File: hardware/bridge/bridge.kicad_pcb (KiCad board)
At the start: 2 copper layers, 45 x 80 mm, 58 parts, among them J1 XT30U-M, J2 Seg A, J3 Seg B, J4 Seg C, J5 Seg D, J6 Head, J7 OLED, J8 Shutdown button, J9 Ext 5V, Q1 NCE40P70K, U1 LMR51606XDBVR, U2 WeAct STM32G474 QFN48, U3 LSM6DSV16X breakout

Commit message: Bridge PCB: soft power switch, PA5 breakout, time-lag fuses
- Soft power switch: Q2 grounds the soft start's R1, so the button (J8,
  now BTN_A and BTN_B) or the bridge's PC4 hold turns the robot on. A
  stretch RC lets a tap last until the bridge has booted; Q3 gives PB5 an
  active-low button sense with no battery voltage on the pin; Q5 and Q4
  snap Q1 off in about 20 ms. Off leaves about 20 uA. JP2, open, bridges
  back to the old always-on behaviour.
- PA5 breakout pads (G 5V 3V3 A5) in the bottom-left corner, name block
  moved below them.
- Data-line zener footprints D4 to D7 dropped to make room; never fitted.
- Segment B and D feeds get a second via at their layer change; SEG C's
  feed runs round the board edge so it no longer walls off the bottom
  layer.
- Fuses changed to BHFUSE BSMD1206C time-lag parts: the Littelfuse 0458s
  were very fast-acting.
- JLC package, PDFs and 3D render regenerated; design note updated
  (docs/bridge-pcb.md section 6.5 has the firmware rules).
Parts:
- removed D4, D5, D6, D7: BZT52C5V6S, Diode_SMD:D_SOD-323
- added C14: 1u 50V, Capacitor_SMD:C_0603_1608Metric, F.Cu at (105.6, 78.9)
- added D11: BAT54WS, Diode_SMD:D_SOD-323, F.Cu at (119.8, 83.9)
- added D12: 1N4148WS, Diode_SMD:D_SOD-323, F.Cu at (102.2, 76.5)
- added D13: BZT52C12S, Diode_SMD:D_SOD-323, F.Cu at (116.1, 83.9)
- added D9: BZT52C12S, Diode_SMD:D_SOD-323, F.Cu at (106.1, 72.0)
- added J10: PA5 breakout, Connector_PinHeader_2.54mm:PinHeader_1x04_P2.54mm_Vertical, F.Cu at (102.0, 115.8)
- added JP2: bridge = always on, Jumper:SolderJumper-2_P1.3mm_Open_RoundedPad1.0x1.5mm, F.Cu at (124.0, 68.6)
- added Q2: 2N7002, Package_TO_SOT_SMD:SOT-23, F.Cu at (120.5, 73.4)
- added Q3: 2N7002, Package_TO_SOT_SMD:SOT-23, F.Cu at (102.3, 73.0)
- added Q4: MMBT3906, Package_TO_SOT_SMD:SOT-23, F.Cu at (112.7, 73.4)
- added Q5: 2N7002, Package_TO_SOT_SMD:SOT-23, F.Cu at (116.6, 73.4)
- added R13: 1M, Resistor_SMD:R_0603_1608Metric, F.Cu at (112.5, 83.7)
- added R14: 470k, Resistor_SMD:R_0603_1608Metric, F.Cu at (105.8, 76.3)
- added R15: 1M, Resistor_SMD:R_0603_1608Metric, F.Cu at (102.1, 78.9)
- added R20: 1M, Resistor_SMD:R_0603_1608Metric, F.Cu at (119.4, 81.6)
- added R21: 2.2M, Resistor_SMD:R_0603_1608Metric, F.Cu at (116.0, 81.6)
- added R22: 1M, Resistor_SMD:R_0603_1608Metric, F.Cu at (112.5, 81.6)
- J8: value Shutdown button -> Power button
- moved R12 7.31 mm to (102.1, 81.1)
- moved D1 7.29 mm to (113.4, 77.1)
- moved C13 7.28 mm to (105.6, 81.1)
- moved R3 7.03 mm to (119.4, 79.6)
- moved R7 6.35 mm to (105.6, 83.2)
- moved R5 5.88 mm to (109.0, 81.1)
- moved R11 5.81 mm to (109.0, 78.9)
- moved D3 5.26 mm to (103.3, 70.1)
- moved R4 5.25 mm to (103.3, 68.2)
- moved C2 3.22 mm to (116.0, 79.6)
- moved R1 2.98 mm to (112.5, 79.6)
- moved R2 2.72 mm to (121.6, 76.7)
- moved R8 2.60 mm to (109.0, 83.2)
- moved R6 2.50 mm to (102.1, 83.2)
- moved C1 2.03 mm to (117.9, 76.9)
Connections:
- J8 pad 1: /BTN -> /BTN_A
- J8 pad 2: GND -> /BTN_B
- R1 pad 2: GND -> /PWR_LO
- U2 pad 36: unconnected-(U2-PC4-Pad36) -> /PWR_HOLD
- U2 pad 37: unconnected-(U2-PA5-Pad37) -> /PA5_IO
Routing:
- net /VHEAD: track 117.2 -> 45.0 mm, vias 4 -> 3
- net /PWR_ON: track 0.00 -> 47.6 mm, vias 0 -> 2
- net /VBAT_F: track 31.5 -> 72.7 mm, vias 4 -> 9
- net /PA5_IO: track 0.00 -> 32.4 mm
- net /BTN_B: track 0.00 -> 29.9 mm, vias 0 -> 1
- net GND: track 284.4 -> 310.4 mm, vias 225 -> 210
- net /LINK_RX: track 99.7 -> 76.5 mm, vias 2 -> 3
- net /PWR_LO: track 0.00 -> 22.3 mm, vias 0 -> 2
- net /Q4_B: track 0.00 -> 16.5 mm, vias 0 -> 2
- net /LINK_TX: track 72.9 -> 89.1 mm
- net +5V: track 44.5 -> 60.4 mm
- net /Q5_G: track 0.00 -> 15.4 mm
- net /OLED_SDA: track 77.9 -> 92.4 mm, vias 4 -> 5
- net /SEG_A: track 46.1 -> 59.8 mm
- net /VBAT_SENSE: track 59.8 -> 47.3 mm, vias 4 -> 1
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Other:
- board text added: "3V3"
- board text added: "A5"
- board text added: "ALWAYS ON"
- board text added: "BRIDGE FOR"

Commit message: Bridge PCB: head feed fuse F6 raised to 2 A
The head carrier's 5 V, 3 A buck draws about 0.85 A from a nearly flat
pack before amplifier peaks, too close to a 1 A rating. F6 is now the
BSMD1206C-1200T (C41367223), same 1206 footprint; fab outputs and the
schematic PDF regenerated, ERC clean.
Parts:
- F6: value 1A -> 2A
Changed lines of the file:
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@@
 			)
 		)
-		(property "Value" "1A"
+		(property "Value" "2A"
 			(at 0 1.83 0)
 			(layer "F.Fab")
@@
 			)
 		)
-		(property "LCSC" "C41367221"
+		(property "LCSC" "C41367223"
 			(at 0 0 0)
 			(layer "F.SilkS")
@@
 			)
 		)
-		(property "MPN" "BHFUSE BSMD1206C-1100T, 1 A time lag, 72 V DC"
+		(property "MPN" "BHFUSE BSMD1206C-1200T, 2 A time lag, 72 V DC"
 			(at 0 0 0)
 			(layer "F.SilkS")

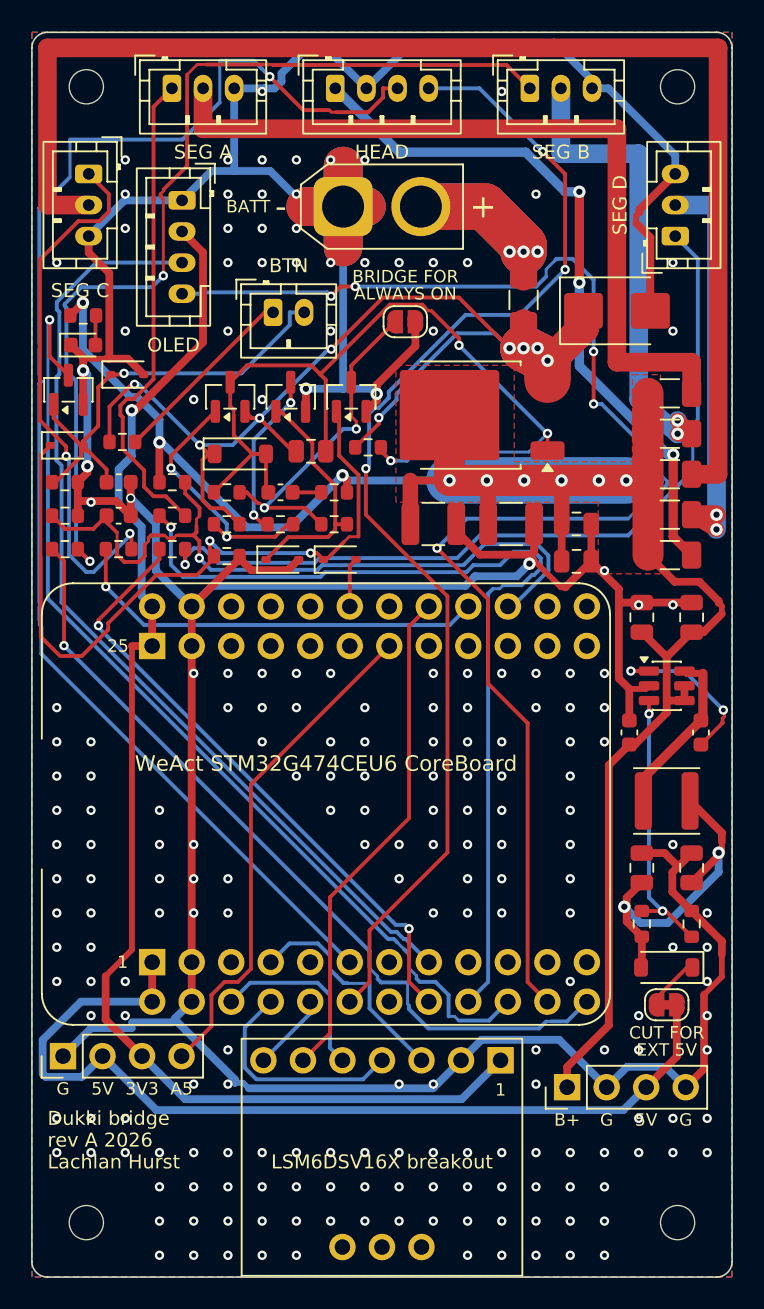
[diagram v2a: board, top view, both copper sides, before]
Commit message: Bridge PCB rev B: WeAct header fix and pre-order review changes
- WeAct footprint: the VCC-side header (P1) had its rows swapped. The
  generator put odd pins on the inner row of both headers, but the two
  headers are the same part placed the same way round, so P1's odd pins
  are on its outer row (confirmed on the board: PB13 is on P1's inner
  row). Every P1 signal would have met its column neighbour.
- J7 (display) is now a 5-pin PH so the 4-pin head cable cannot go in it.
- C15, 1 uF X7R on PWR_ON: holds the power switch through a bridge reset
  and stretches a tap; C14 now X7R 0805, R14 220k.
- L1 SWPA6045S330MT (1.65 A saturation), D2 SMBJ26A (C19077580,
  Preferred).
- Buck column re-laid in current order; bulk capacitors stood on end
  under Q1; power capacitor ground pads solid; head feed VHEAD in a
  1.0 mm class.
- JP1 turned 180 degrees with hand-drawn links, and a top-layer keep-out
  across its cut line (no tracks, vias or pour).
- NYLON marked at H1 and H2 (segment C's feed runs under their heads).
- Routing tidied with tidy_head_pcb.py; DRC clean with schematic parity.
  JLC package, PDFs and render regenerated; design note section 6.6.
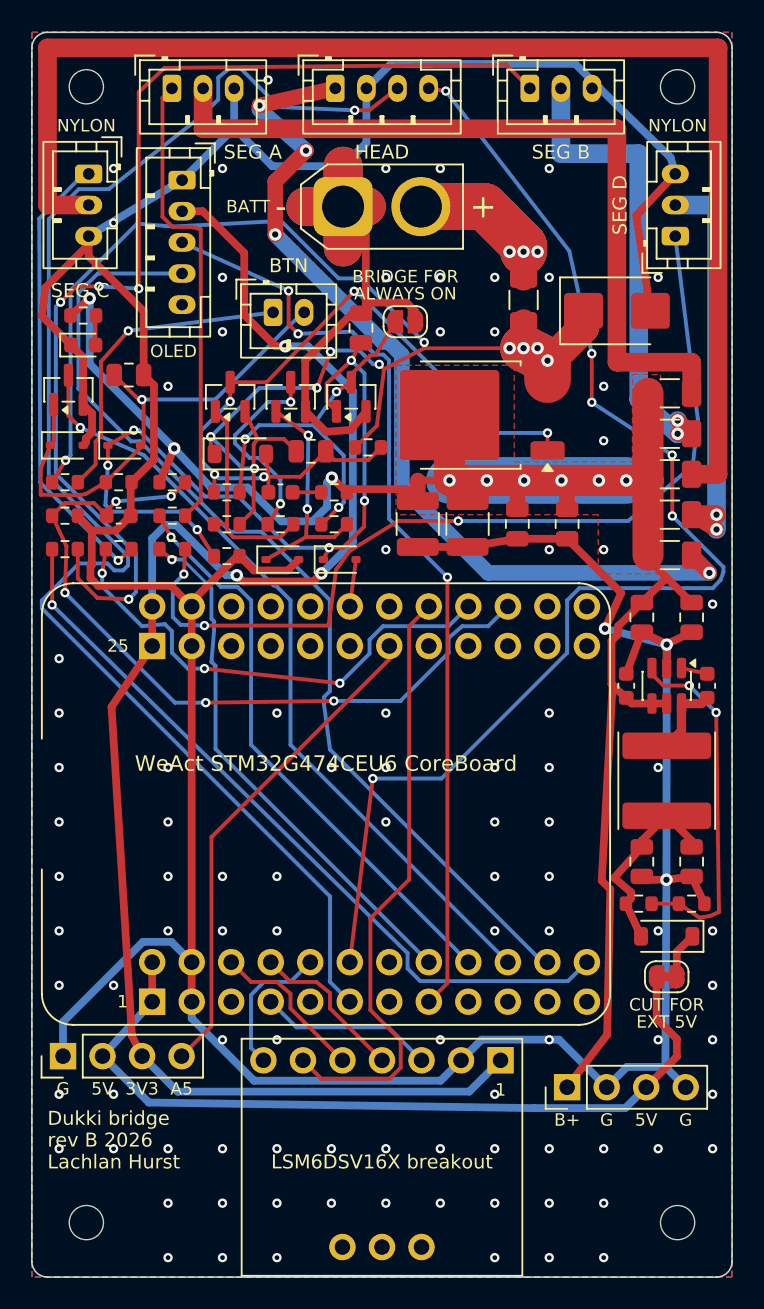
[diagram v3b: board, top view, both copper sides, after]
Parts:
- added C15: 1u 50V X7R, Capacitor_SMD:C_0805_2012Metric, F.Cu at (121.2, 69.0)
- C14: value 1u 50V -> 1u 50V X7R; footprint Capacitor_SMD:C_0603_1608Metric -> Capacitor_SMD:C_0805_2012Metric
- D2: value SMBJ30A -> SMBJ26A
- J7: footprint Connector_JST:JST_PH_B4B-PH-K_1x04_P2.00mm_Vertical -> Connector_JST:JST_PH_B5B-PH-K_1x05_P2.00mm_Vertical
- L1: footprint Inductor_SMD:L_Sunlord_SWPA4030S -> Inductor_SMD:L_Sunlord_SWPA6045S
- R14: value 470k -> 220k
- moved C14 6.92 mm to (106.2, 72.0)
- moved D9 5.99 mm to (102.2, 76.5)
- moved R14 4.51 mm to (102.1, 78.9)
- moved C5 3.80 mm to (131.2, 81.6), turned to -90 degrees
- moved D12 3.69 mm to (105.9, 76.5)
- moved R15 3.45 mm to (105.6, 78.9)
- moved C9 3.03 mm to (143.4, 92.0), turned to -90 degrees
- moved C10 3.01 mm to (138.2, 92.0)
- moved C4 2.80 mm to (128.0, 81.6), turned to -90 degrees
- moved C6 2.47 mm to (134.4, 81.6), turned to -90 degrees
- moved D8 2.00 mm to (140.8, 108.1)
- moved JP1 1.80 mm to (140.8, 110.7), turned to 180 degrees
- moved R9 1.32 mm to (139.0, 106.0), turned to 0 degrees
- moved L1 1.30 mm to (140.8, 98.1), turned to -90 degrees
- moved J7 1.30 mm to (109.7, 59.5)
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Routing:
- net /OLED_SDA: track 92.4 -> 64.5 mm, vias 5 -> 0
- net /VBAT_F: track 72.7 -> 96.7 mm, vias 9 -> 11
- net /SEG_A: track 59.8 -> 37.4 mm
- net +3V3: track 85.0 -> 102.7 mm, vias 1 -> 3
- net /BTN: track 64.8 -> 50.5 mm
- net /VHEAD: track 45.0 -> 58.9 mm, vias 3 -> 4
- net /5V_BUCK: track 22.4 -> 12.6 mm, vias 2 -> 0
- net /SEG_B_C: track 62.0 -> 71.7 mm, vias 2 -> 4
- net /BUCK_CB: track 11.0 -> 1.69 mm, vias 2 -> 0
- net /BTN_A: track 12.3 -> 20.4 mm, vias 0 -> 1
- net +5V: track 60.4 -> 52.5 mm
- net GND: track 310.4 -> 303.2 mm, vias 210 -> 98
- net /IMU_CS: track 32.5 -> 39.1 mm
- net /Q1_G: track 56.8 -> 50.6 mm, vias 3 -> 5
- net /BUCK_SW: track 11.0 -> 4.91 mm
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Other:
- board text added: "NYLON"
- board text added: "rev B 2026"
- board text removed: "rev A 2026"

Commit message: Bridge PCB: module pin labels and ground marks on the silkscreen
- Pin labels for the WeAct board in its own silkscreen style (two lines
  per column between the header rows, the upper line naming the upper
  row) and for the LSM6DSV16X breakout beside each pin, from the new
  scripts/kicad/module_labels.py. They lie under the modules once fitted,
  for checking orientation as each goes on.
- A G beside the ground pin of each segment connector, outside the
  housing: a reversed pigtail swaps SIGNAL and GND.
- Silkscreen only, no copper changes; DRC clean with schematic parity.
  JLC package, layout PDF and render regenerated.
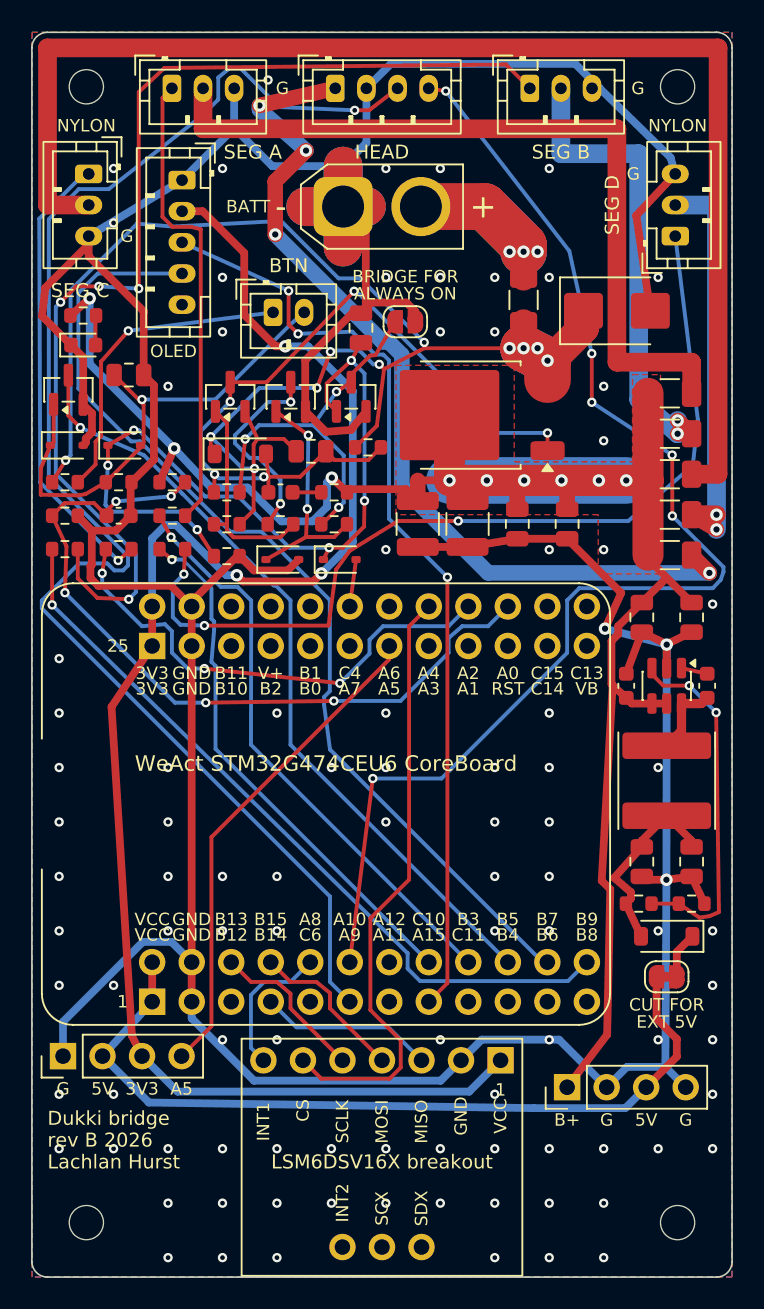
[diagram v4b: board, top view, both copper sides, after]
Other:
- board text added: "A0"
- board text added: "A1"
- board text added: "A10"
- board text added: "A11"
- board text added: "A12"
- board text added: "A15"
- board text added: "A2"
- board text added: "A3"
- board text added: "A4"
- board text added: "A6"
- board text added: "A7"
- board text added: "A8"
- board text added: "A9"
- board text added: "B0"
- board text added: "B1"
- board text added: "B10"
- board text added: "B11"
- board text added: "B12"
- board text added: "B13"
- board text added: "B14"
- board text added: "B15"
- board text added: "B2"
- board text added: "B3"
- board text added: "B4"
- board text added: "B5"
- board text added: "B6"
- board text added: "B7"
- board text added: "B8"
- board text added: "B9"
- board text added: "C10"
- board text added: "C11"
- board text added: "C13"
- board text added: "C14"
- board text added: "C15"
- board text added: "C4"
- board text added: "C6"
- board text added: "CS"
- board text added: "GND"
- board text added: "INT1"
- board text added: "INT2"
- board text added: "MISO"
- board text added: "MOSI"
- board text added: "RST"
- board text added: "SCLK"
- board text added: "SCX"
- board text added: "SDX"
- board text added: "V+"
- board text added: "VB"
- board text added: "VCC"

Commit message: Bridge PCB: pin names inside the head and display connector outlines
- J6 (head: B+, G, TX, RX) and J7 (display: G, 3V3, SCL, SDA, NC) get
  their pin names on the front silkscreen inside the housing outlines,
  in 0.6 mm text to fit between the pads and the outline. Hidden once
  the connectors are fitted; a reference on an unpopulated board.
- The board's minimum silkscreen text height is lowered to 0.5 mm for
  them (JLC recommends 0.8 to 1.0 mm, so they print a little soft).
- Silkscreen only, no copper changes; DRC clean with schematic parity.
  Gerbers and layout PDF regenerated.
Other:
- board text added: "NC"
- board text added: "RX"
- board text added: "SCL"
- board text added: "SDA"
- board text added: "TX"
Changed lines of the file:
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@@
 		(layer "Edge.Cuts")
+	)
+	(gr_text "B+"
+		(at 119.5 54.95 0)
+		(layer "F.SilkS")
+		(effects
+			(font
+				(size 0.6 0.6)
+				(thickness 0.12)
+			)
+		)
+	)
+	(gr_text "G"
+		(at 121.5 54.95 0)
+		(layer "F.SilkS")
+		(effects
+			(font
+				(size 0.6 0.6)
+				(thickness 0.12)
+			)
+		)
+	)
+	(gr_text "TX"
+		(at 123.5 54.95 0)
+		(layer "F.SilkS")
+		(effects
+			(font
+				(size 0.6 0.6)
+				(thickness 0.12)
+			)
+		)
+	)
+	(gr_text "RX"
+		(at 125.5 54.95 0)
+		(layer "F.SilkS")
+		(effects
+			(font
+				(size 0.6 0.6)
+				(thickness 0.12)
+			)
+		)
+	)
+	(gr_text "G"
+		(at 108.3 59.5 90)
+		(layer "F.SilkS")
+		(effects
+			(font
+				(size 0.6 0.6)
+				(thickness 0.12)
+			)
+		)
+	)
+	(gr_text "3V3"
+		(at 108.3 61.5 90)
+		(layer "F.SilkS")
+		(effects
+			(font
+				(size 0.6 0.6)
+				(thickness 0.12)
+			)
+		)
+	)
+	(gr_text "SCL"
+		(at 108.3 63.5 90)
+		(layer "F.SilkS")
+		(effects
+			(font
+				(size 0.6 0.6)
+				(thickness 0.12)
+			)
+		)
+	)
+	(gr_text "SDA"
+		(at 108.3 65.5 90)
+		(layer "F.SilkS")
+		(effects
+			(font
+				(size 0.6 0.6)
+				(thickness 0.12)
+			)
+		)
+	)
+	(gr_text "NC"
+		(at 108.3 67.5 90)
+		(layer "F.SilkS")
+		(effects
+			(font
+				(size 0.6 0.6)
+				(thickness 0.12)
+			)
+		)
 	)
 	(gr_text "3V3"
